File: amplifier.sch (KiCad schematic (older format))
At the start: 0 parts

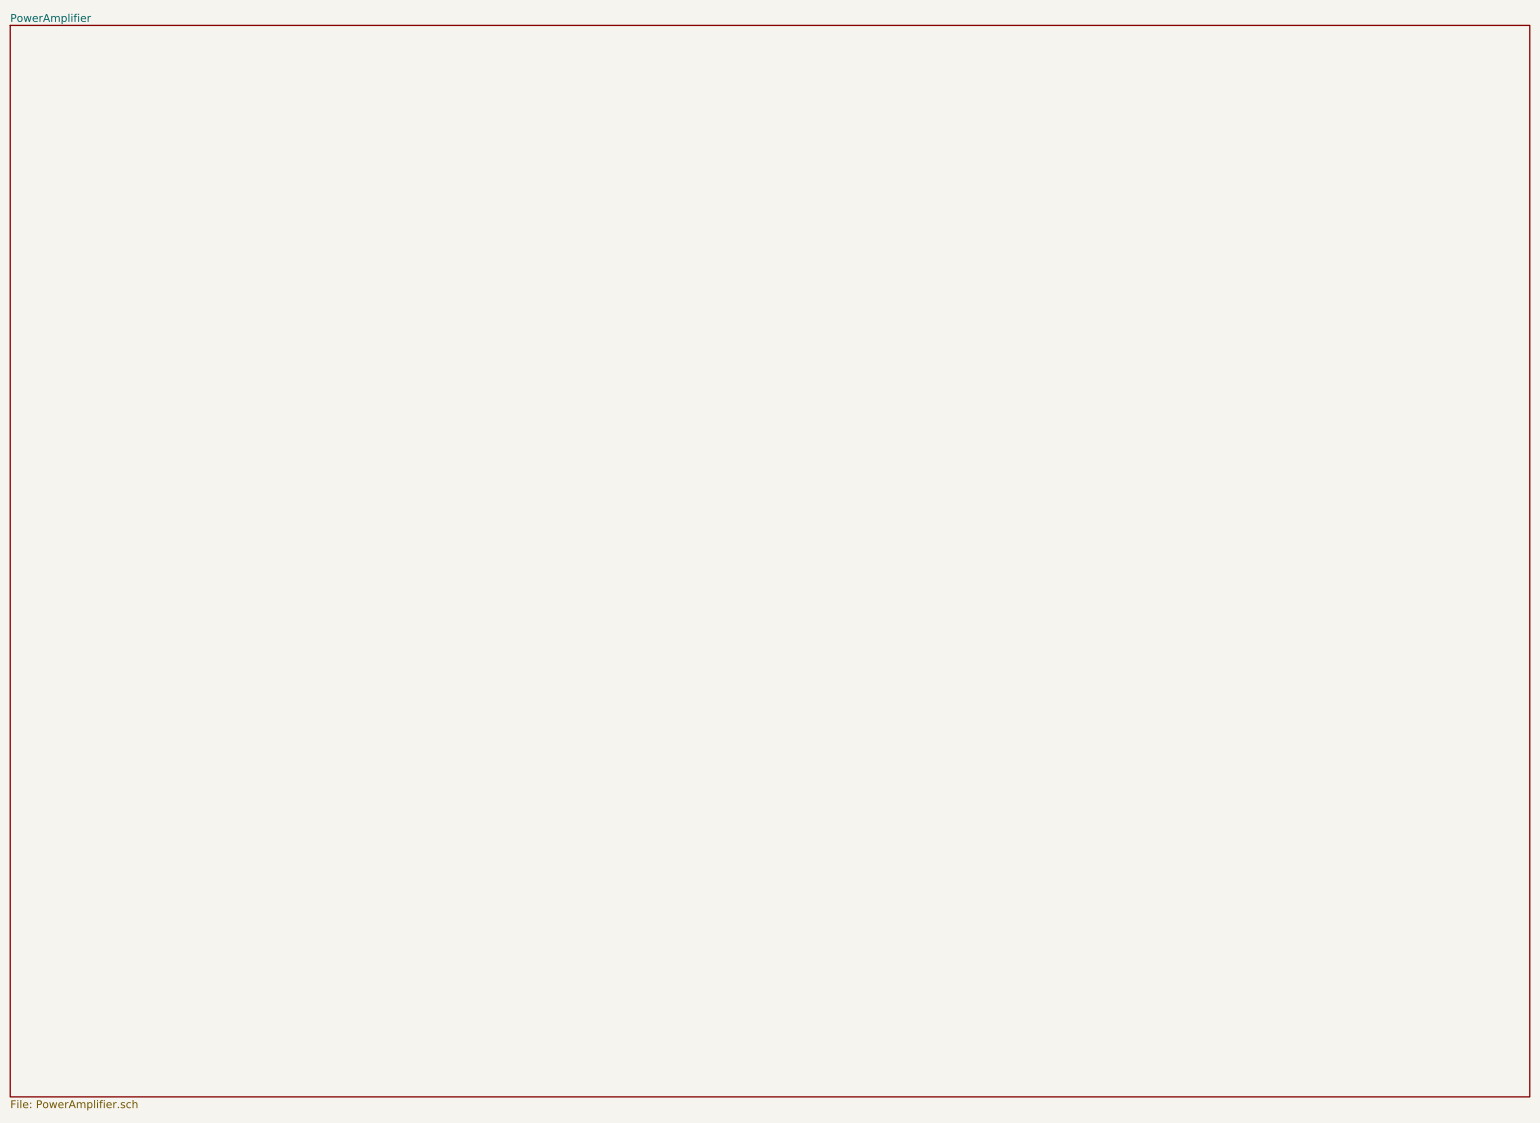
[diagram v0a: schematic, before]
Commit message: Add SatelitesPowerAmplifier scheme
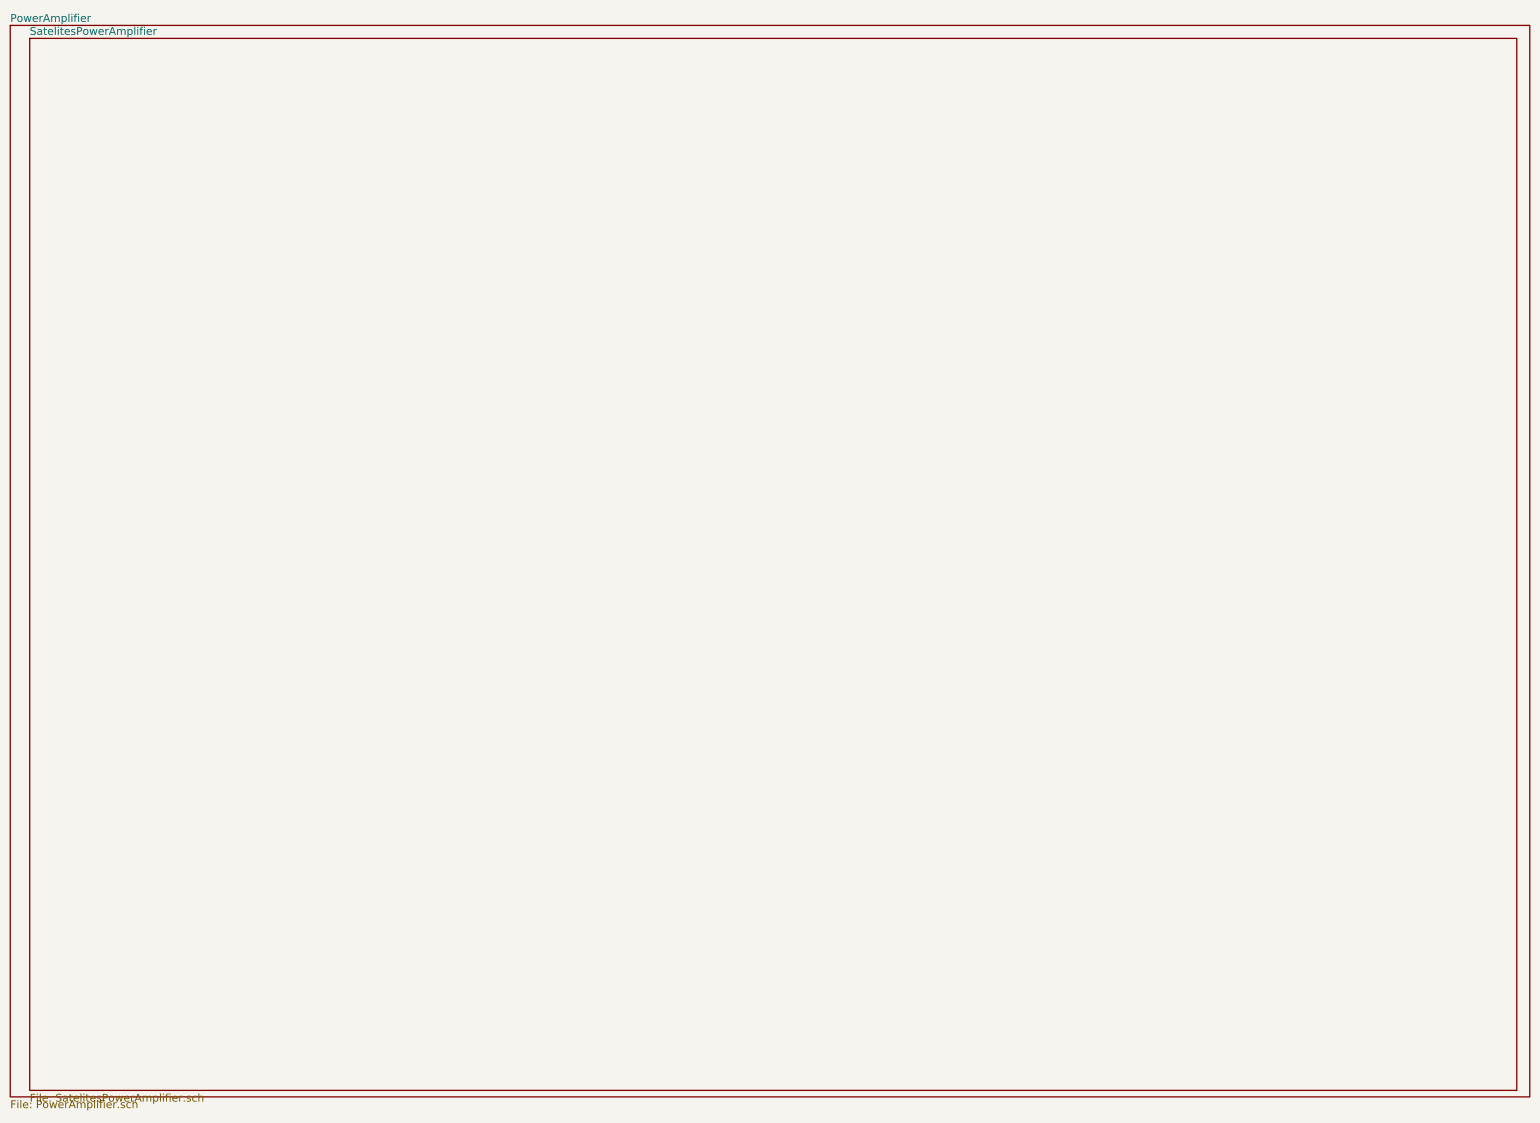
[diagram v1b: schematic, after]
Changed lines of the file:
@@
 EESchema Schematic File Version 2
+LIBS:amplifier-rescue
 LIBS:power
 LIBS:device
@@
 LIBS:tda7293v
 LIBS:amplifier-cache
-EELAYER 25 0
+EELAYER 26 0
 EELAYER END
 $Descr A4 11693 8268
 encoding utf-8
-Sheet 1 2
+Sheet 1 3
 Title ""
 Date ""
@@
 F1 "PowerAmplifier.sch" 60
 $EndSheet
+$Sheet
+S 150  100  11450 8100
+U 588A0618
+F0 "SatelitesPowerAmplifier" 60
+F1 "SatelitesPowerAmplifier.sch" 60
+$EndSheet
 $EndSCHEMATC
